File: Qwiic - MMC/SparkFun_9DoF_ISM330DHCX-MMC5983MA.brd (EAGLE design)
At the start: 25.4 x 25.4 mm, 71 parts, among them J1 QWIIC_RIGHT_ANGLE, J2 QWIIC_RIGHT_ANGLE, U1 ISM330DHCX, U2 MMC5983MA_QFN16

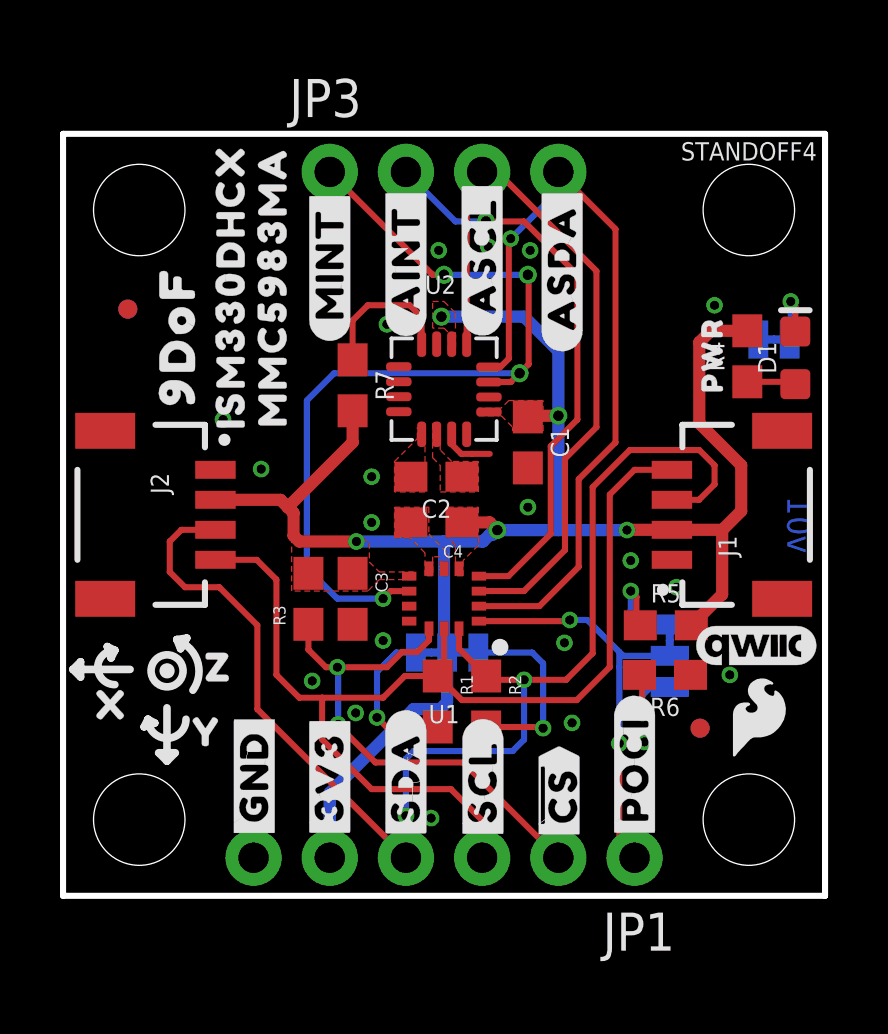
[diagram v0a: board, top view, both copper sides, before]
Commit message: Restricts ground pour around Magnetometer, renames 6DoF I2C nets
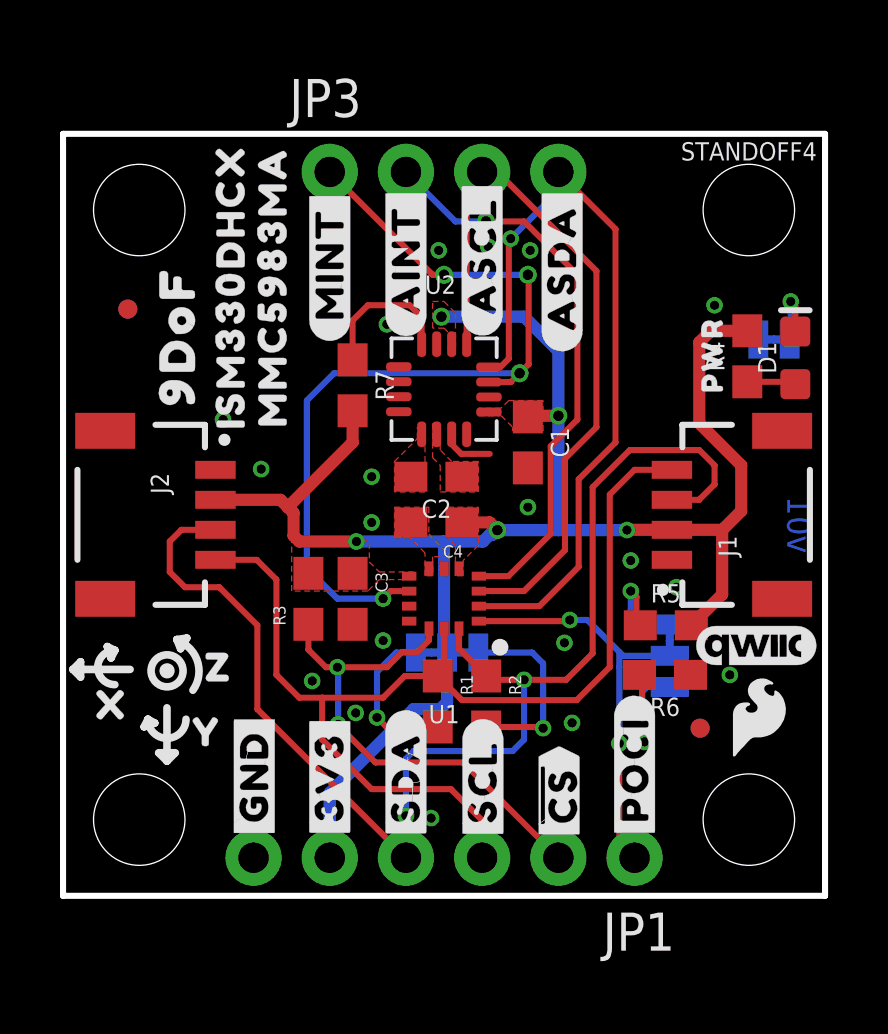
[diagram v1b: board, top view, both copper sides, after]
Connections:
- net ISM_SCL renamed MAG_SCL
- net ISM_SDA renamed MAG_SDA
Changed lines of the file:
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@@
 <layer number="39" name="tKeepout" color="4" fill="11" visible="no" active="yes"/>
 <layer number="40" name="bKeepout" color="1" fill="11" visible="no" active="yes"/>
-<layer number="41" name="tRestrict" color="4" fill="10" visible="no" active="yes"/>
+<layer number="41" name="tRestrict" color="4" fill="10" visible="yes" active="yes"/>
 <layer number="42" name="bRestrict" color="1" fill="10" visible="no" active="yes"/>
 <layer number="43" name="vRestrict" color="2" fill="10" visible="no" active="yes"/>
@@
 <rectangle x1="12.9032" y1="15.875" x2="12.954" y2="16.1798" layer="41" rot="R90"/>
 <rectangle x1="11.8872" y1="15.875" x2="11.938" y2="16.1798" layer="41" rot="R90"/>
+<rectangle x1="11.8872" y1="15.875" x2="11.938" y2="16.1798" layer="41" rot="R90"/>
+<rectangle x1="11.5062" y1="15.4432" x2="11.557" y2="15.748" layer="41" rot="R180"/>
 </plain>
 <attributes>
@@
 <contactref element="R6" pad="2"/>
 <contactref element="6DOF_ADDR" pad="1"/>
-<wire x1="20.22475" y1="6.9596" x2="19.58975" y2="6.9596" width="0.2032" layer="16"/>
-<wire x1="19.58975" y1="6.9596" x2="19.304" y2="6.67385" width="0.2032" layer="16"/>
-<wire x1="19.304" y1="6.096" x2="19.304" y2="6.67385" width="0.2032" layer="16"/>
+<wire x1="20.22475" y1="6.9596" x2="19.46275" y2="6.9596" width="0.2032" layer="16"/>
+<wire x1="19.46275" y1="6.9596" x2="19.304" y2="6.80085" width="0.2032" layer="16"/>
+<wire x1="19.304" y1="6.096" x2="19.304" y2="6.80085" width="0.2032" layer="16"/>
 <via x="19.304" y="6.096" extent="1-16" drill="0.3048"/>
 <wire x1="19.304" y1="6.096" x2="19.304" y2="7.278" width="0.2032" layer="1"/>
 <wire x1="19.304" y1="7.278" x2="19.216" y2="7.366" width="0.2032" layer="1"/>
 </signal>
-<signal name="ISM_SCL">
+<signal name="MAG_SCL">
 <contactref element="U1" pad="P3"/>
 <contactref element="JP3" pad="3"/>
@@
 <wire x1="11.684" y1="4.826" x2="14.986" y2="4.826" width="0.2032" layer="16"/>
 </signal>
-<signal name="ISM_SDA">
+<signal name="MAG_SDA">
 <contactref element="U1" pad="P2"/>
 <contactref element="JP3" pad="4"/>

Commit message: Fixes many silk errors
* Adds polarity marker to MMC - previous one is eaten by PTH silk
* Adds flags to interrupt silk
* Moves resistor to make room for SDA and SCL silk
* Renames "MAG SDA/SCL"  net to "AUX SDA/SCL"
* Rotates version number in copper
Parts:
- removed U$12: (no value), top:#MINT#14
- removed U$35: (no value), ISMTopMini:Y2115
- removed U$36, U$39: (no value), ISMTopMini:Z2116
- added U$33: (no value), top:#0X6A#15
- added U$40: (no value), top:#0X6B#15
- U$13: device bot:#0X6A#11 -> top:ACC#Z5985
- U$14: device bot:#0X6B#11 -> top:MAG#Z5984
- U$34: device ISMTopMini:X2114 -> top:#MINT#14
- U$7: device top:#MAG_INT#12 -> top:#AINT#13
- U$8: device top:#AINT#13 -> top:#MAG_INT#12
- moved U$34 16.4 mm to (8.89, 21.1), turned to 90 degrees
- moved U$13 7.97 mm to (16.0, 15.1)
- moved U$7 2.90 mm to (11.4, 21.2), flipped to the top, turned to 90 degrees
- moved U$8 2.90 mm to (8.89, 19.8), flipped to the bottom, turned to 270 degrees
- moved U$14 2.83 mm to (16.0, 11.2)
- moved U$37 1.27 mm to (10.4, 14.1)
- moved U$38 1.27 mm to (13.6, 13.1)
- moved R2 1.14 mm to (15.2, 6.48)
- moved R1 0.25 mm to (12.7, 6.48)
- moved U$6 0.13 mm to (18.8, 4.22)
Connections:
- net MAG_SCL renamed AUX_SCL
- net MAG_SDA renamed AUX_SDA
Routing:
- net GND: vias 20 -> 25

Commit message: Changes main 6DoF to new part
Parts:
- U1: value ISM330DHCX -> ISM330DLC; device ISM330DHCX:LGA-14L -> ISM330DLC:LGA-14L
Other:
- board text added: "Elias Santistevan"
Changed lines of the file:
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@@
 <layer number="37" name="tTest" color="7" fill="1" visible="no" active="yes"/>
 <layer number="38" name="bTest" color="7" fill="1" visible="no" active="yes"/>
-<layer number="39" name="tKeepout" color="4" fill="11" visible="yes" active="yes"/>
+<layer number="39" name="tKeepout" color="4" fill="11" visible="no" active="yes"/>
 <layer number="40" name="bKeepout" color="1" fill="11" visible="no" active="yes"/>
-<layer number="41" name="tRestrict" color="4" fill="10" visible="yes" active="yes"/>
+<layer number="41" name="tRestrict" color="4" fill="10" visible="no" active="yes"/>
 <layer number="42" name="bRestrict" color="1" fill="10" visible="no" active="yes"/>
 <layer number="43" name="vRestrict" color="2" fill="10" visible="no" active="yes"/>
@@
 <circle x="12.4079" y="11.18235" radius="0.127" width="0.254" layer="22"/>
 <circle x="12.4079" y="11.18235" radius="0.5334" width="0.254" layer="22"/>
+<text x="11.557" y="-20.447" size="1.778" layer="51" font="vector">Elias Santistevan</text>
 </plain>
 <attributes>
@@
 </element>
 <element name="U$29" library="SparkFun-Aesthetics" package="SFE_LOGO_FLAME_.1" value="" x="23.1902" y="5.969" smashed="yes"/>
-<element name="U1" library="ISM330DHCX" package="LGA-14L" value="ISM330DHCX" x="12.7" y="9.906" smashed="yes" rot="R180">
+<element name="U1" library="ISM330DLC" package="LGA-14L" value="ISM330DLC" x="12.7" y="9.906" smashed="yes" rot="R180">
 <attribute name="NAME" x="12.7" y="6.057" size="0.6096" layer="25" font="vector" ratio="20" rot="R180" align="center"/>
 <attribute name="PROD_ID" value="IC-16693" x="12.7" y="9.906" size="1.778" layer="27" rot="R180" display="off"/>
@@
 <via x="13.8938" y="5.8928" extent="1-16" drill="0.3048"/>
 <via x="14.6558" y="4.1148" extent="1-16" drill="0.3048"/>
+<wire x1="21.717" y1="19.685" x2="23.1775" y2="18.542" width="0" layer="19" extent="16-16"/>
+<wire x1="15.5702" y1="21.5138" x2="21.717" y2="19.685" width="0" layer="19" extent="1-1"/>
+<wire x1="14.1732" y1="21.6408" x2="15.5702" y2="21.5138" width="0" layer="19" extent="1-1"/>
+<wire x1="12.5222" y1="21.5138" x2="14.1732" y2="21.6408" width="0" layer="19" extent="1-1"/>
+<wire x1="10.795" y1="19.05" x2="12.5222" y2="21.5138" width="0" layer="19" extent="1-1"/>
+<wire x1="11.954" y1="15.385" x2="10.795" y2="19.05" width="0" layer="19" extent="1-1"/>
+<wire x1="12.954" y1="15.385" x2="11.954" y2="15.385" width="0" layer="19" extent="1-1"/>
+<wire x1="11.954" y1="14.328" x2="11.954" y2="15.385" width="0" layer="19" extent="1-1"/>
+<wire x1="10.287" y1="13.97" x2="11.596" y2="13.97" width="0" layer="19" extent="1-1"/>
+<wire x1="15.494" y1="14.263" x2="14.224" y2="14.732" width="0" layer="19" extent="1-1"/>
+<wire x1="15.494" y1="12.954" x2="15.494" y2="14.263" width="0" layer="19" extent="1-1"/>
+<wire x1="11.596" y1="12.446" x2="11.596" y2="13.97" width="0" layer="19" extent="1-1"/>
+<wire x1="10.287" y1="12.446" x2="11.596" y2="12.446" width="0" layer="19" extent="1-1"/>
+<wire x1="12.2" y1="10.906" x2="11.596" y2="12.446" width="0" layer="19" extent="1-1"/>
+<wire x1="12.7" y1="10.906" x2="12.2" y2="10.906" width="0" layer="19" extent="1-1"/>
+<wire x1="10.668" y1="8.509" x2="12.2" y2="10.906" width="0" layer="19" extent="1-1"/>
+<wire x1="9.652" y1="9.04965" x2="10.668" y2="8.509" width="0" layer="19" extent="1-1"/>
+<wire x1="8.3058" y1="7.1628" x2="9.652" y2="9.04965" width="0" layer="19" extent="1-1"/>
+<wire x1="7.7978" y1="5.8928" x2="8.3058" y2="7.1628" width="0" layer="19" extent="1-1"/>
+<wire x1="9.7536" y1="6.096" x2="8.3058" y2="7.1628" width="0" layer="19" extent="1-1"/>
+<wire x1="6.5278" y1="8.1788" x2="8.3058" y2="7.1628" width="0" layer="19" extent="1-1"/>
+<wire x1="10.4648" y1="2.9718" x2="9.7536" y2="6.096" width="0" layer="19" extent="1-1"/>
+<wire x1="12.2682" y1="2.5908" x2="10.4648" y2="2.9718" width="0" layer="19" extent="1-1"/>
+<wire x1="14.6558" y1="4.1148" x2="12.2682" y2="2.5908" width="0" layer="19" extent="1-1"/>
+<wire x1="13.8938" y1="5.8928" x2="14.6558" y2="4.1148" width="0" layer="19" extent="1-1"/>
+<wire x1="17.4752" y1="5.6388" x2="14.6558" y2="4.1148" width="0" layer="19" extent="1-1"/>
+<wire x1="19.3802" y1="5.1308" x2="17.4752" y2="5.6388" width="0" layer="19" extent="1-1"/>
+<wire x1="20.916" y1="7.366" x2="19.3802" y2="5.1308" width="0" layer="19" extent="1-1"/>
+<wire x1="22.225" y1="7.366" x2="20.916" y2="7.366" width="0" layer="19" extent="1-1"/>
+<wire x1="16.7132" y1="8.4328" x2="17.4752" y2="5.6388" width="0" layer="19" extent="1-1"/>
+<wire x1="20.447" y1="10.287" x2="20.916" y2="7.366" width="0" layer="19" extent="1-1"/>
+<wire x1="20.2946" y1="11.2" x2="20.447" y2="10.287" width="0" layer="19" extent="1-1"/>
+<wire x1="18.923" y1="11.176" x2="20.2946" y2="11.2" width="0" layer="19" extent="1-1"/>
+<wire x1="6.604" y1="14.224" x2="10.287" y2="13.97" width="0" layer="19" extent="1-1"/>
+<wire x1="5.08" y1="14.2" x2="6.604" y2="14.224" width="0" layer="19" extent="1-1"/>
+<wire x1="5.334" y1="15.875" x2="5.08" y2="14.2" width="0" layer="19" extent="1-1"/>
+<wire x1="6.35" y1="1.27" x2="10.4648" y2="2.9718" width="0" layer="19" extent="1-1"/>
 </signal>
 <signal name="SCL">
@@
 <wire x1="7.874" y1="11.811" x2="7.6835" y2="12.0015" width="0.4064" layer="1"/>
 <wire x1="7.6835" y1="12.0015" x2="7.6835" y2="12.7635" width="0.4064" layer="1"/>
+<wire x1="12.6116" y1="19.304" x2="12.954" y2="18.389" width="0" layer="19" extent="1-1"/>
+<wire x1="9.652" y1="10.74965" x2="9.779" y2="11.811" width="0" layer="19" extent="1-1"/>
+<wire x1="14.196" y1="16.127" x2="15.494" y2="15.963" width="0" layer="19" extent="1-1"/>
+<wire x1="8.1788" y1="10.74965" x2="9.652" y2="10.74965" width="0" layer="19" extent="1-1"/>
+<wire x1="13.2" y1="10.906" x2="13.296" y2="12.446" width="0" layer="19" extent="1-1"/>
+<wire x1="11.5375" y1="10.656" x2="13.2" y2="10.906" width="0" layer="19" extent="1-1"/>
 </signal>
 <signal name="N$5">
